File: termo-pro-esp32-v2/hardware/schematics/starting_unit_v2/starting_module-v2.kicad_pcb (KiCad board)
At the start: 2 copper layers, 120 x 65 mm, 22 parts, among them J1 Screw_Terminal_01x02, J2 Screw_Terminal_01x02, J3 Conn_01x08_Pin, K1 SANYOU_SRD_Form_C, Q1 PN2222A, SW1 SW_Push_LED, U2 ESP32-C3_SUPERMINI_TH

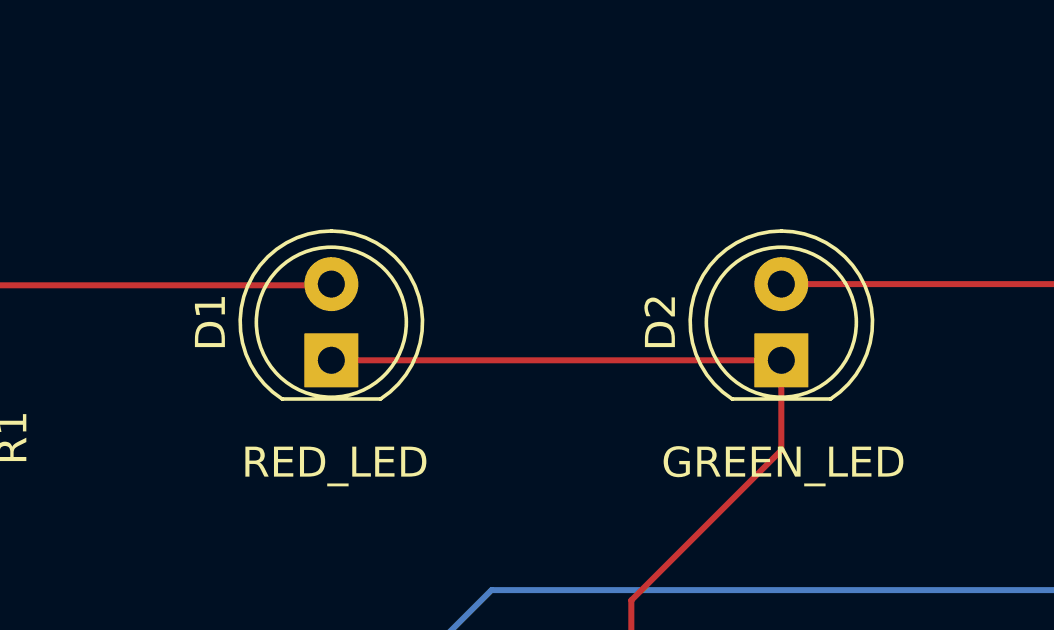
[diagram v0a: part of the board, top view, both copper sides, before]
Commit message: Removed circular LED and replaced them with rectangular ones.
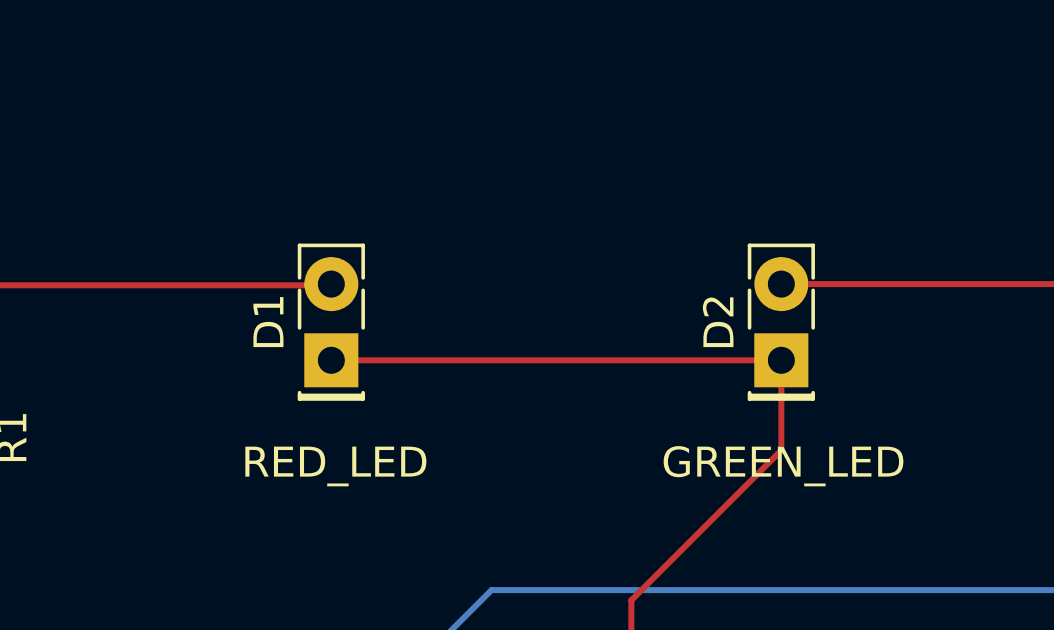
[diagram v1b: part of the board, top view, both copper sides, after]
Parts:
- D1, D2: footprint LED_THT:LED_D5.0mm_FlatTop -> LED_THT:LED_Rectangular_W5.0mm_H2.0mm
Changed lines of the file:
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@@
 			(drillshape 0)
 			(scaleselection 1)
-			(outputdirectory "../../../pcb/Drill Files/Starting Unit/")
+			(outputdirectory "../../pcb/drill_files/starting_unit/")
 		)
 	)
@@
 		)
 	)
-	(footprint "LED_THT:LED_D5.0mm_FlatTop"
+	(footprint "LED_THT:LED_Rectangular_W5.0mm_H2.0mm"
 		(layer "F.Cu")
 		(at 195 63 90)
-		(descr "LED, Round, Flat Top, diameter 5.0mm, 2 pins, https://www.kingbright.com/attachments/file/psearch/000/00/watermark00/L-483GDT(Ver.12B).pdf, generated by kicad-footprint-generator")
+		(descr "LED, Rectangular, size 5.0x2.0mm, 2 pins, http://www.kingbright.com/attachments/file/psearch/000/00/00/L-169XCGDK(Ver.9B).pdf, generated by kicad-footprint-generator")
 		(tags "LED")
 		(property "Reference" "D2"
-			(at 1.27 -4.01 90)
+			(at 1.27 -2.06 90)
 			(layer "F.SilkS")
 			(effects
@@
 		)
 		(property "Value" "LED"
-			(at 1.27 4.01 90)
+			(at 1.27 2.06 90)
 			(layer "F.Fab")
 			(effects
@@
 		(duplicate_pad_numbers_are_jumpers no)
 		(fp_line
-			(start -1.29 -1.64)
-			(end -1.29 1.64)
+			(start 3.83 -1.06)
+			(end 3.83 1.06)
 			(stroke
 				(width 0.12)
@@
 			(layer "F.SilkS")
 		)
-		(fp_arc
-			(start -1.29 -1.639512)
-			(mid 2.124166 -2.917533)
-			(end 4.31 0)
+		(fp_line
+			(start 2.747 -1.06)
+			(end 3.83 -1.06)
 			(stroke
 				(width 0.12)
@@
 			(layer "F.SilkS")
 		)
-		(fp_arc
-			(start 4.31 0)
-			(mid 2.124166 2.917533)
-			(end -1.29 1.639512)
+		(fp_line
+			(start 1.08 -1.06)
+			(end 2.333 -1.06)
 			(stroke
 				(width 0.12)
@@
 			(layer "F.SilkS")
 		)
-		(fp_circle
-			(center 1.27 0)
-			(end 3.77 0)
+		(fp_line
+			(start -1.17 -1.06)
+			(end -1.17 1.06)
 			(stroke
 				(width 0.12)
 				(type solid)
 			)
-			(fill no)
 			(layer "F.SilkS")
 		)
-		(fp_rect
-			(start -2 -3.26)
-			(end 4.53 3.26)
+		(fp_line
+			(start -1.29 -1.06)
+			(end -1.08 -1.06)
 			(stroke
-				(width 0.05)
+				(width 0.12)
 				(type solid)
 			)
-			(fill no)
-			(layer "F.CrtYd")
+			(layer "F.SilkS")
 		)
 		(fp_line
-			(start -1.23 -1.566046)
-			(end -1.23 1.566046)
+			(start 3.83 1.06)
+			(end 2.747 1.06)
 			(stroke
-				(width 0.1)
+				(width 0.12)
 				(type solid)
 			)
-			(layer "F.Fab")
+			(layer "F.SilkS")
 		)
-		(fp_arc
-			(start -1.23 -1.566046)
-			(mid 4.22 0)
-			(end -1.23 1.566046)
+		(fp_line
+			(start 2.333 1.06)
+			(end 1.08 1.06)
 			(stroke
-				(width 0.1)
+				(width 0.12)
 				(type solid)
 			)
-			(layer "F.Fab")
+			(layer "F.SilkS")
 		)
-		(fp_circle
-			(center 1.27 0)
-			(end 3.77 0)
+		(fp_line
+			(start -1.08 1.06)
+			(end -1.29 1.06)
+			(stroke
+				(width 0.12)
+				(type solid)
+			)
+			(layer "F.SilkS")
+		)
+		(fp_line
+			(start -1.29 1.06)
+			(end -1.29 -1.06)
+			(stroke
+				(width 0.12)
+				(type solid)
+			)
+			(layer "F.SilkS")
+		)
+		(fp_rect
+			(start -1.54 -1.31)
+			(end 4.08 1.31)
+			(stroke
+				(width 0.05)
+				(type solid)
+			)
+			(fill no)
+			(layer "F.CrtYd")
+		)
+		(fp_rect
+			(start -1.23 -1)
+			(end 3.77 1)
 			(stroke
 				(width 0.1)
@@
 		)
 		(embedded_fonts no)
-		(model "${KICAD10_3DMODEL_DIR}/LED_THT.3dshapes/LED_D5.0mm_FlatTop.step"
+		(model "${KICAD10_3DMODEL_DIR}/LED_THT.3dshapes/LED_Rectangular_W5.0mm_H2.0mm.step"
 			(offset
 				(xyz 0 0 0)
@@
 		(embedded_fonts no)
 	)
-	(footprint "LED_THT:LED_D5.0mm_FlatTop"
+	(footprint "LED_THT:LED_Rectangular_W5.0mm_H2.0mm"
 		(layer "F.Cu")
 		(at 180 63 90)
-		(descr "LED, Round, Flat Top, diameter 5.0mm, 2 pins, https://www.kingbright.com/attachments/file/psearch/000/00/watermark00/L-483GDT(Ver.12B).pdf, generated by kicad-footprint-generator")
+		(descr "LED, Rectangular, size 5.0x2.0mm, 2 pins, http://www.kingbright.com/attachments/file/psearch/000/00/00/L-169XCGDK(Ver.9B).pdf, generated by kicad-footprint-generator")
 		(tags "LED")
 		(property "Reference" "D1"
-			(at 1.27 -4.01 90)
+			(at 1.27 -2.06 90)
 			(layer "F.SilkS")
 			(effects
@@
 		)
 		(property "Value" "LED"
-			(at 1.27 4.01 90)
+			(at 1.27 2.06 90)
 			(layer "F.Fab")
 			(effects
@@
 		(duplicate_pad_numbers_are_jumpers no)
 		(fp_line
-			(start -1.29 -1.64)
-			(end -1.29 1.64)
+			(start 3.83 -1.06)
+			(end 3.83 1.06)
 			(stroke
 				(width 0.12)
@@
 			(layer "F.SilkS")
 		)
-		(fp_arc
-			(start -1.29 -1.639512)
-			(mid 2.124166 -2.917533)
-			(end 4.31 0)
+		(fp_line
+			(start 2.747 -1.06)
+			(end 3.83 -1.06)
 			(stroke
 				(width 0.12)
@@
 			(layer "F.SilkS")
 		)
-		(fp_arc
-			(start 4.31 0)
-			(mid 2.124166 2.917533)
-			(end -1.29 1.639512)
+		(fp_line
+			(start 1.08 -1.06)
+			(end 2.333 -1.06)
 			(stroke
 				(width 0.12)
@@
 			(layer "F.SilkS")
 		)
-		(fp_circle
-			(center 1.27 0)
-			(end 3.77 0)
+		(fp_line
+			(start -1.17 -1.06)
+			(end -1.17 1.06)
 			(stroke
 				(width 0.12)
 				(type solid)
 			)
-			(fill no)
 			(layer "F.SilkS")
 		)
-		(fp_rect
-			(start -2 -3.26)
-			(end 4.53 3.26)
+		(fp_line
+			(start -1.29 -1.06)
+			(end -1.08 -1.06)
 			(stroke
-				(width 0.05)
+				(width 0.12)
 				(type solid)
 			)
-			(fill no)
-			(layer "F.CrtYd")
+			(layer "F.SilkS")
 		)
 		(fp_line
-			(start -1.23 -1.566046)
-			(end -1.23 1.566046)
+			(start 3.83 1.06)
+			(end 2.747 1.06)
 			(stroke
-				(width 0.1)
+				(width 0.12)
 				(type solid)
 			)
-			(layer "F.Fab")
+			(layer "F.SilkS")
 		)
-		(fp_arc
-			(start -1.23 -1.566046)
-			(mid 4.22 0)
-			(end -1.23 1.566046)
+		(fp_line
+			(start 2.333 1.06)
+			(end 1.08 1.06)
 			(stroke
-				(width 0.1)
+				(width 0.12)
 				(type solid)
 			)
-			(layer "F.Fab")
+			(layer "F.SilkS")
 		)
-		(fp_circle
-			(center 1.27 0)
-			(end 3.77 0)
+		(fp_line
+			(start -1.08 1.06)
+			(end -1.29 1.06)
+			(stroke
+				(width 0.12)
+				(type solid)
+			)
+			(layer "F.SilkS")
+		)
+		(fp_line
+			(start -1.29 1.06)
+			(end -1.29 -1.06)
+			(stroke
+				(width 0.12)
+				(type solid)
+			)
+			(layer "F.SilkS")
+		)
+		(fp_rect
+			(start -1.54 -1.31)
+			(end 4.08 1.31)
+			(stroke
+				(width 0.05)
+				(type solid)
+			)
+			(fill no)
+			(layer "F.CrtYd")
+		)
+		(fp_rect
+			(start -1.23 -1)
+			(end 3.77 1)
 			(stroke
 				(width 0.1)
@@
 		)
 		(embedded_fonts no)
-		(model "${KICAD10_3DMODEL_DIR}/LED_THT.3dshapes/LED_D5.0mm_FlatTop.step"
+		(model "${KICAD10_3DMODEL_DIR}/LED_THT.3dshapes/LED_Rectangular_W5.0mm_H2.0mm.step"
 			(offset
 				(xyz 0 0 0)
@@
 	)
 	(segment
+		(start 192 91)
+		(end 191.27 90.27)
+		(width 0.2)
+		(layer "F.Cu")
+		(net "Net-(Q1-B)")
+	)
+	(segment
+		(start 191.27 90.27)
+		(end 191.27 82)
+		(width 0.2)
+		(layer "F.Cu")
+		(net "Net-(Q1-B)")
+	)
+	(segment
 		(start 211.16 76.635)
 		(end 211.16 80)
@@
 	)
 	(segment
-		(start 192 91)
-		(end 191.27 90.27)
-		(width 0.2)
-		(layer "F.Cu")
-		(net "Net-(Q1-B)")
-	)
-	(segment
-		(start 191.27 90.27)
-		(end 191.27 82)
-		(width 0.2)
-		(layer "F.Cu")
-		(net "Net-(Q1-B)")
-	)
-	(segment

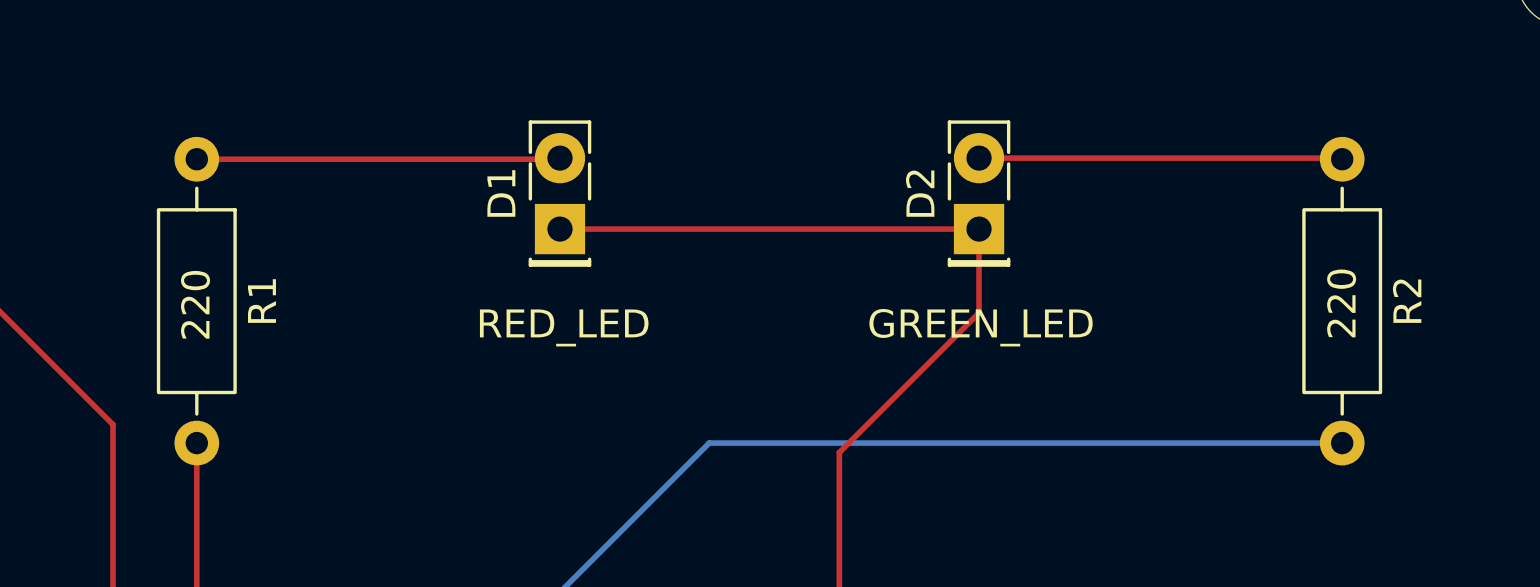
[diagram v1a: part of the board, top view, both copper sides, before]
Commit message: Documentation changes
Starting unit schematic and PCB has been updated for the 50 ohm resistors used for LED.
gerber and drill files generated again.
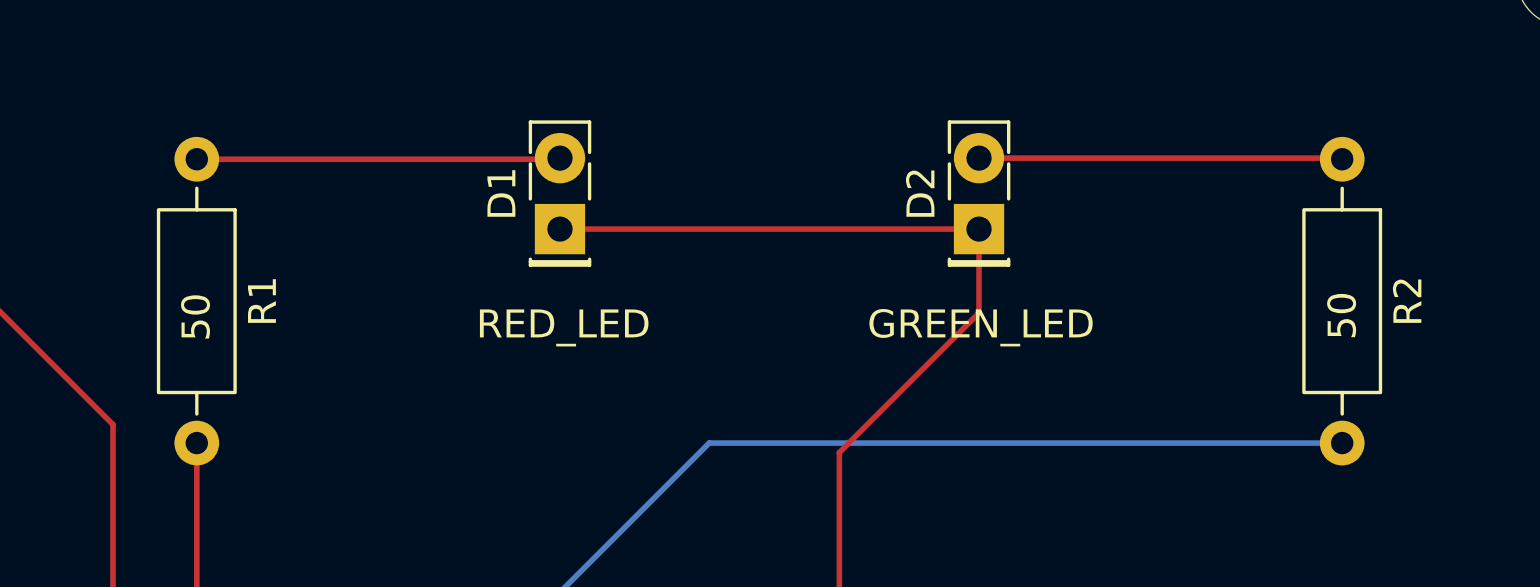
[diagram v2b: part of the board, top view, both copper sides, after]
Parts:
- R1, R2: value 220 -> 50
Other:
- board text added: "50"
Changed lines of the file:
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@@
 			)
 		)
-		(property "Value" "220"
+		(property "Value" "50"
 			(at 5.08 2.37 90)
 			(layer "F.Fab")
@@
 			)
 		)
-		(property "Value" "220"
+		(property "Value" "50"
 			(at 5.08 2.37 90)
 			(layer "F.Fab")
@@
 		)
 	)
-	(gr_text "220"
+	(gr_text "50"
 		(at 167.575 67.025 90)
 		(layer "F.SilkS")
@@
 		)
 	)
-	(gr_text "220"
+	(gr_text "50"
 		(at 208.6 66.975 90)
 		(layer "F.SilkS")
